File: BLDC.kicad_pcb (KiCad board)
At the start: 4 copper layers, 60 x 60 mm, 113 parts, among them J1 43650-0510, J2 436500313, J3 TC2030-MCP-NL, J4 43650-0510, U0 LSM6DS3US, U1 LMZ21700SILT, U12 MCP9808, U13 AS5047U, U17 INA250, U18 INA250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

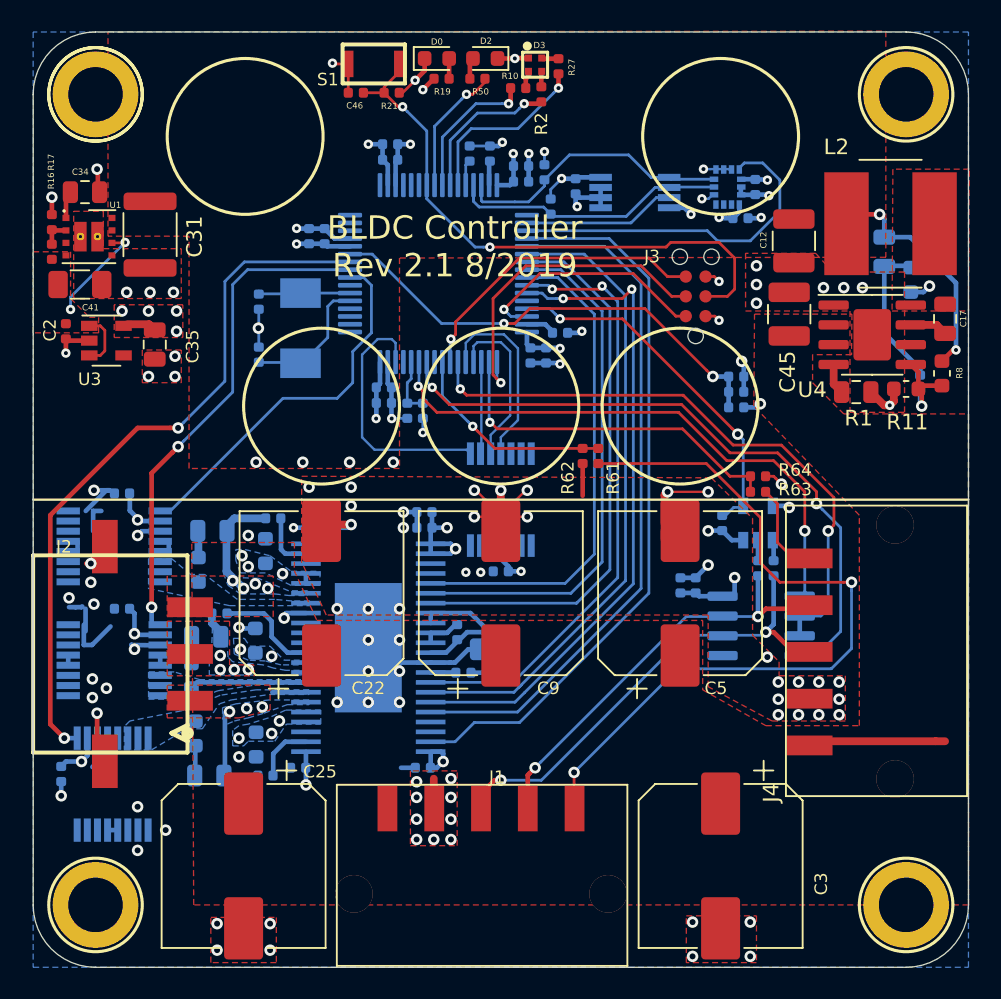
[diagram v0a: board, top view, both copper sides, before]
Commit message: switch to larger accel package. enlarge all vias and traces. clean up.
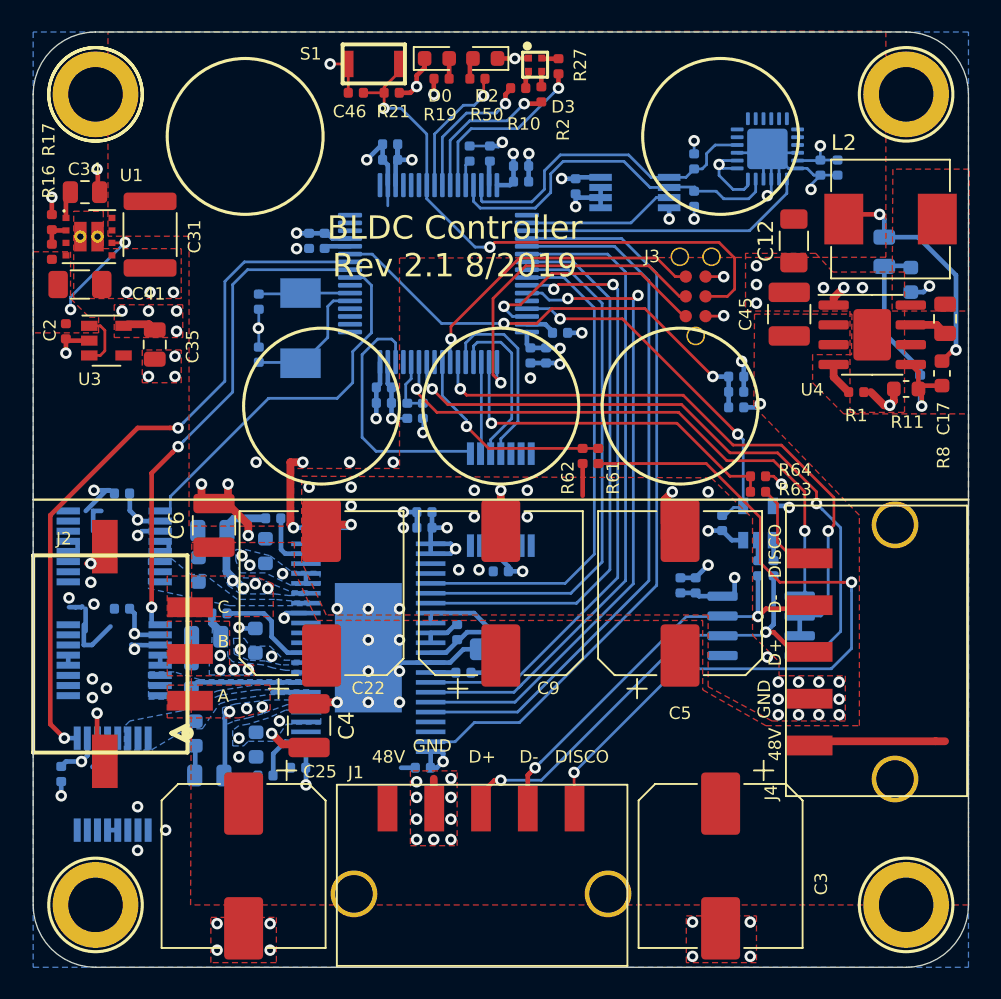
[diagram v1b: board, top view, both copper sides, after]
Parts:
- removed U0: LSM6DS3US, BLDC:LGA-14L
- added C4: 4u7, Capacitor_SMD:C_1210_3225Metric, F.Cu at (136.2, 119.5)
- added C6: 4u7, Capacitor_SMD:C_1210_3225Metric, F.Cu at (130.1, 106.7)
- added U2: IIS328DQ, Package_DFN_QFN:QFN-24-1EP_4x4mm_P0.5mm_EP2.6x2.6mm, B.Cu at (165.6, 82.5)
- C12: footprint Capacitor_SMD:C_1210_3225Metric -> Capacitor_SMD:C_1206_3216Metric
- C45: value 2u2 -> 4u7
- L2: value 100 uH -> 82 uH; footprint Inductor_SMD:L_Bourns_SRN8040TA -> Inductor_SMD:L_7.3x7.3_H4.5
- R1: value 100k -> 40k2; footprint Resistor_SMD:R_0805_2012Metric -> Resistor_SMD:R_0402_1005Metric
- R7: value 237k -> 255k
- U1: value LMZ21700SILT -> LMZ21700SIL
- moved R39 9.63 mm to (160.9, 83.3)
- moved R9 9.21 mm to (160.9, 85.7), turned to 270 degrees
- moved C20 7.02 mm to (170.1, 83.7), turned to 90 degrees
- moved C21 4.36 mm to (169.0, 83.7)
- moved C38 0.30 mm to (136.2, 88.4)
- moved C40 0.30 mm to (137.2, 88.4)
- moved L2 0.30 mm to (173.5, 87.0)
- renumbered XTAL0 to X0
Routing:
- net GND: track 112.9 -> 120.0 mm, vias 108 -> 110
- net /I2C_SCL: track 17.6 -> 23.5 mm
- net +3V3: track 55.7 -> 61.1 mm
- net +12V: track 30.0 -> 35.4 mm
- net /IMU_INT1: track 22.6 -> 18.6 mm
- net /I2C_SDA: track 18.1 -> 20.9 mm
- net +48V: track 10.4 -> 12.8 mm
- net /MOT_OCTW: track 47.0 -> 47.9 mm
- net /MOT_RST_A: track 41.4 -> 42.3 mm
- net /MOT_FAULT: track 44.7 -> 45.5 mm
- net /MOT_PWM_B: track 38.9 -> 39.5 mm
- net /ISENSE_C: track 23.4 -> 24.0 mm
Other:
- net class 3v3Power: clearance 0.1524 -> 0.1778; trace_width 0.1524 -> 0.1778; via_dia 0.6 -> 0.74; via_drill 0.254 -> 0.38
- net class 48vPower: via_drill 0.35 -> 0.38
- net class Default: clearance 0.1524 -> 0.1778; trace_width 0.1524 -> 0.1778; via_dia 0.6 -> 0.74; via_drill 0.254 -> 0.38
- net class Test Points: clearance 0.1524 -> 0.1778; trace_width 0.1524 -> 0.1778; via_drill 0.254 -> 0.38
- rule trace_clearance: 0.1524 -> 0.1778
- rule trace_min: 0.152 -> 0.1778
- rule via_min_size: 0.6 -> 0.7
- board text added: "48V"
- board text added: "A"
- board text added: "B"
- board text added: "C"
- board text added: "D+"
- board text added: "D-"
- board text added: "DISCO"
- board text added: "GND"

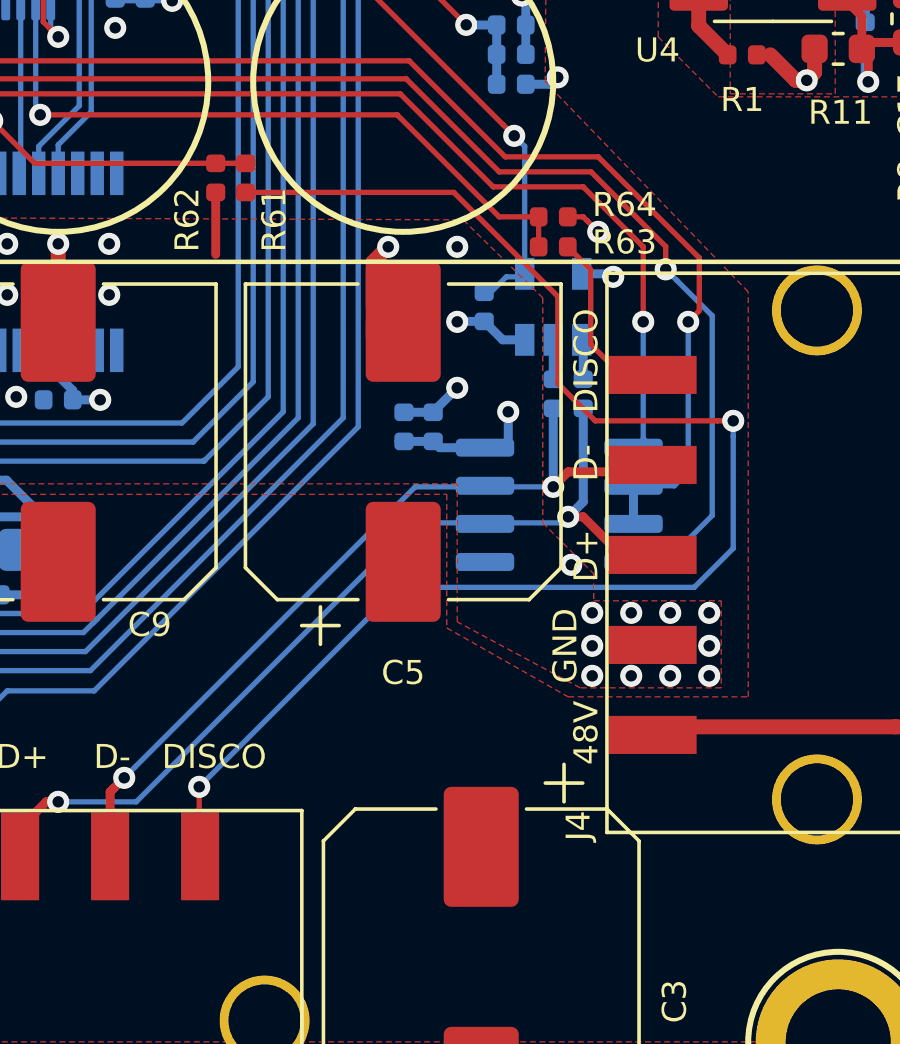
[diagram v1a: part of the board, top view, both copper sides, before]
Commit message: Adding In/Out labels to Molex Connectors
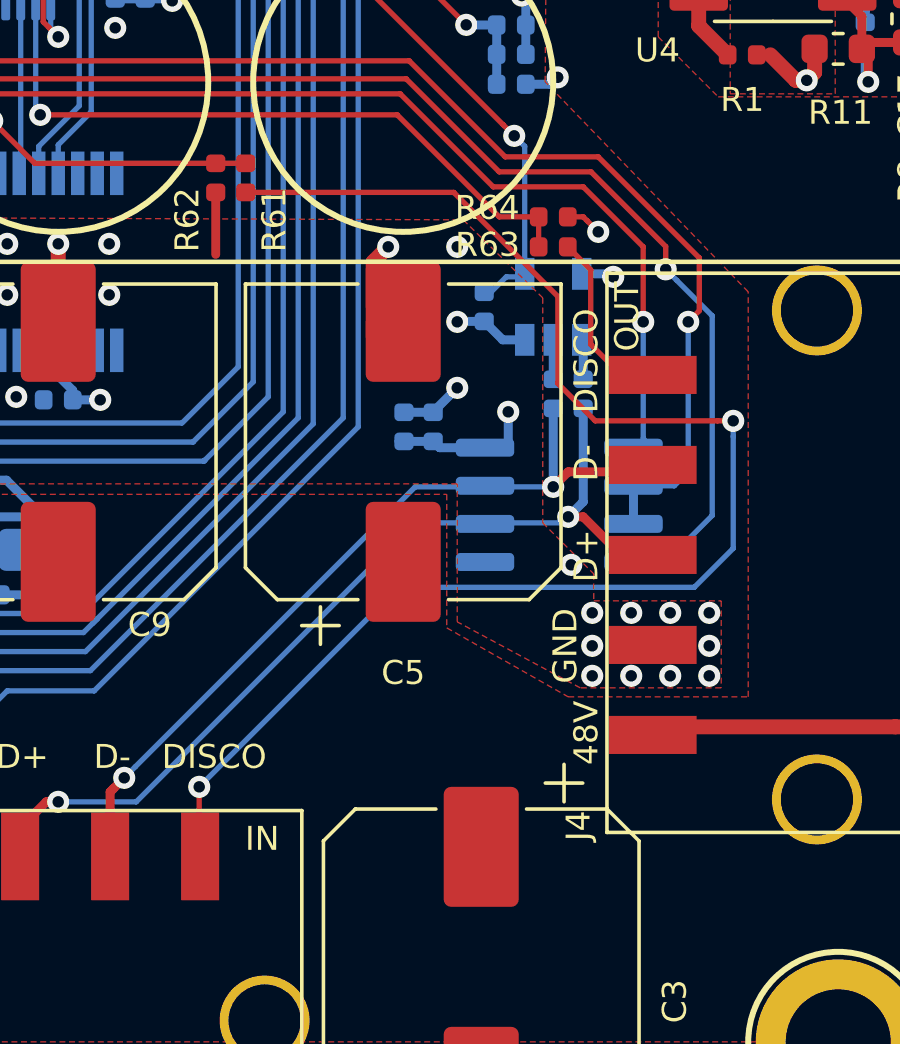
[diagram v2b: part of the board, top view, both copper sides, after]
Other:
- board text added: "IN"
- board text added: "OUT"

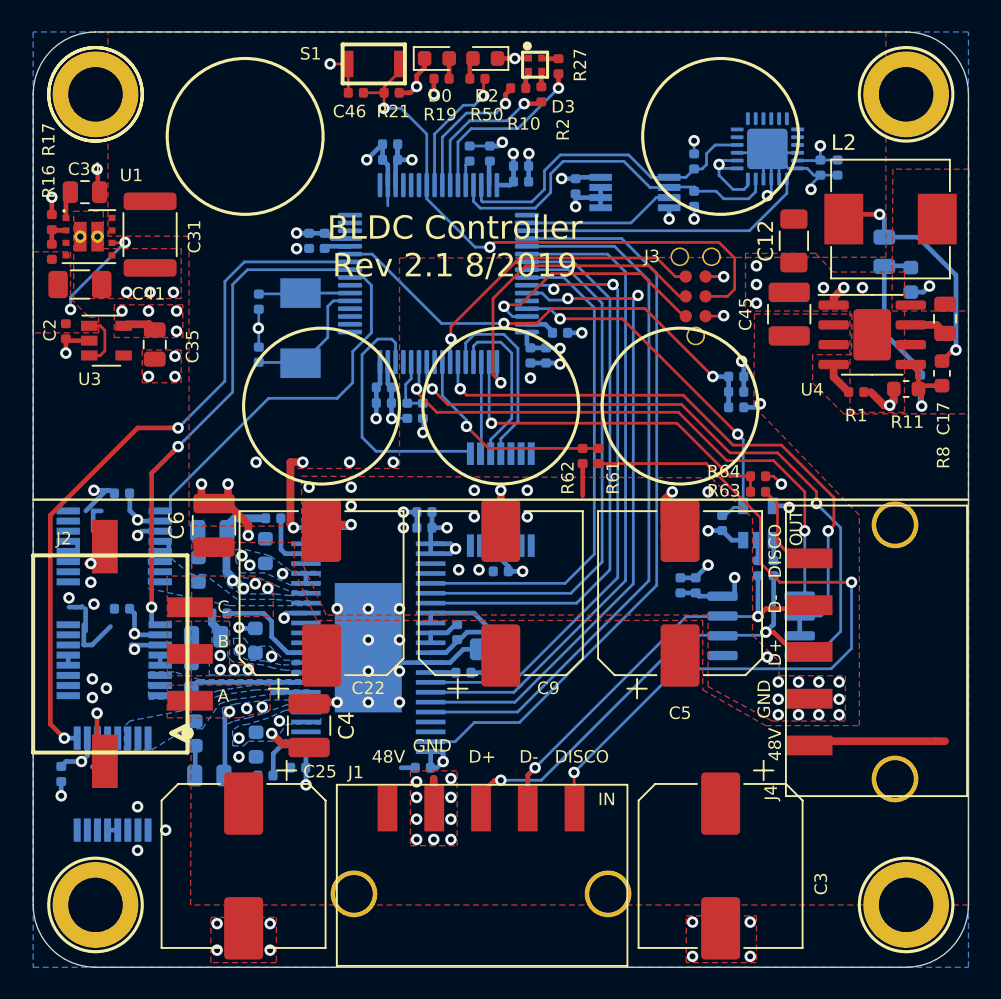
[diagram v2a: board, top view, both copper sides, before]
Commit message: use NRST for SWD_RESET
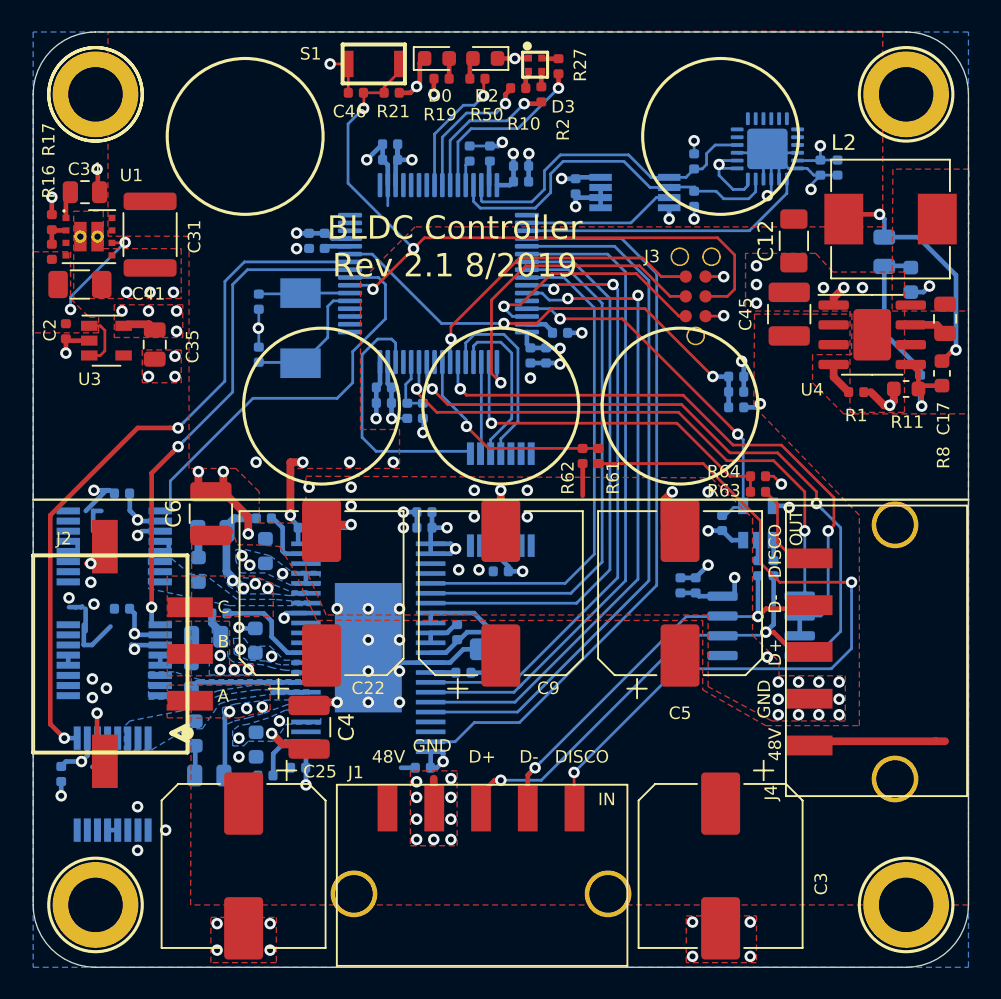
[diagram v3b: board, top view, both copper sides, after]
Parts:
- moved C6 0.78 mm to (129.9, 105.9)
- moved C56 0.60 mm to (133.3, 106.2)
- moved C61 0.51 mm to (136.0, 106.8)
- moved C4 0.10 mm to (136.2, 119.6)
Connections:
- U9 pad 23: /SWD_RESET -> Net-(U9-Pad23)
- U9 pad 7: Net-(U9-Pad7) -> /SWD_RESET
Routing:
- net /SWD_RESET: track 37.8 -> 46.6 mm, vias 2 -> 3
- net GND: track 120.0 -> 122.1 mm
- net /ISENSE_C: track 24.0 -> 25.9 mm
- net +12V: track 35.4 -> 34.7 mm
- net /driver_phase-C: track 7.16 -> 6.46 mm

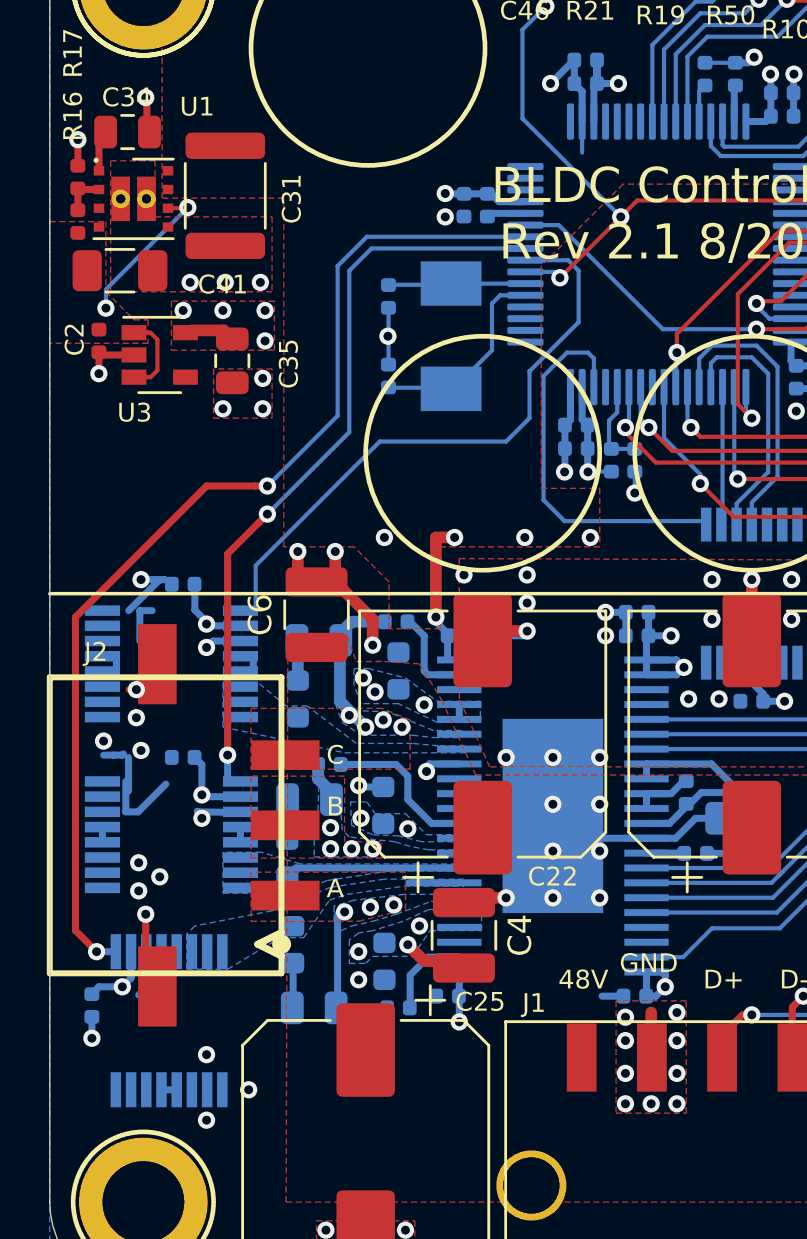
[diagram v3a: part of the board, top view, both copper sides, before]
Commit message: add 1v2 reference to INA250 and MCU ADC
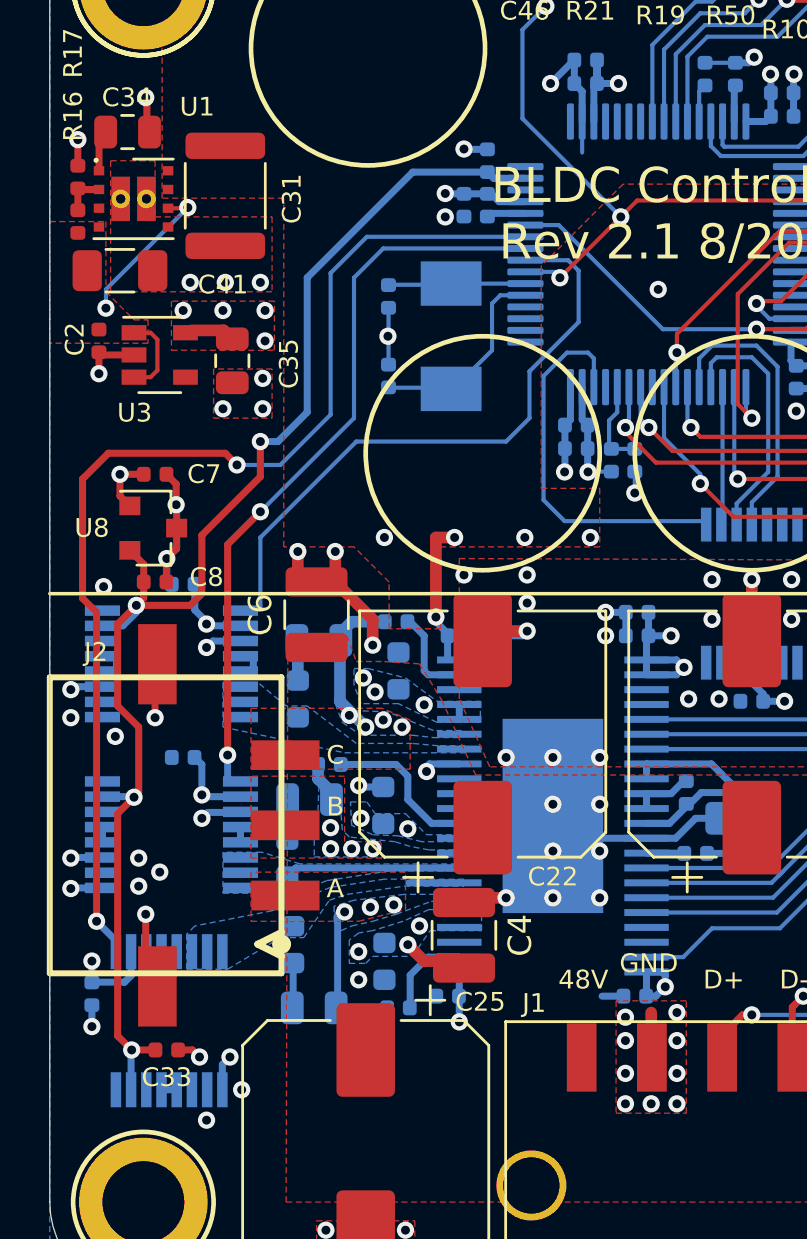
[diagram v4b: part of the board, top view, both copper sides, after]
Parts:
- added C33: 1u, Capacitor_SMD:C_0402_1005Metric, F.Cu at (123.5, 124.5)
- added C37: 100n, Capacitor_SMD:C_0402_1005Metric, B.Cu at (137.2, 86.5)
- added C7: 100n, Capacitor_SMD:C_0402_1005Metric, F.Cu at (123.0, 99.9)
- added C8: 1u, Capacitor_SMD:C_0402_1005Metric, F.Cu at (123.0, 104.5)
- added U8: REF3312AIDBZ, Package_TO_SOT_SMD:SOT-23, F.Cu at (122.9, 102.2)
- C13, C14, C16, C19, C24, C26, C40, C63: value 100.0nF -> 100n
- C27, C30, C38, C48, C67: value 1.0μF -> 1u
- C47, C49: value 2.2μF -> 2u2
- C54, C57: value 27.0pF -> 27p
- R39, R9: value 2.21kΩ -> 2k21
- R56: value 47.0kΩ -> 47k
- moved C16 0.50 mm to (120.3, 122.1)
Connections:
- U17 pad 7: GND -> +1V2
- U18 pad 7: GND -> +1V2
- U19 pad 7: GND -> +1V2
- U9 pad 15: Net-(U9-Pad15) -> +1V2
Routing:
- net +1V2: track 0.00 -> 59.2 mm, vias 0 -> 4
- net +3V3: track 61.1 -> 64.2 mm, vias 24 -> 25
- net GND: track 122.1 -> 125.0 mm, vias 110 -> 117
- net /ISENSE_A: track 45.2 -> 48.0 mm
- net /ISENSE_C: track 25.9 -> 26.5 mm

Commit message: Added BOM
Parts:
- R1: footprint Resistor_SMD:R_0402_1005Metric -> Resistor_SMD:R_0805_2012Metric
